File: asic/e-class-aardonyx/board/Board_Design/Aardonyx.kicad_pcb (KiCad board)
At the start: 4 copper layers, 157.5 x 117.3 mm, 325 parts, among them J1 USB_B_6PIN, J10 Conn_1x6_F, J11 Conn_1x6_F, J12 Conn_1x3_M, J13 Conn_1x8_F, J14 Conn_1x6_F, J15 Conn_1x10, J16 Conn_1x8_F, J17 USB_OTG, J18 Conn_1x3_M, J19 Conn_1x3_M, J2 Conn_1x8, J3 Conn_1x3_M, J4 Conn_1x4, J5 PJ-202H PWRJACK, J6 Conn_1x3_M, J7 Conn_1x4, J8 Conn_1x3_M, J9 Conn_1x8, Q1 FDN339AN, SW1 SW_SPST, SW2 FSM2JSMAATR, SW3 SW_DIP_x03, U1 FT2232H, U10 TPS7A7002DDAR, U11 ADM1186, U13 TPS7A7002DDAR, U14 74AUP1G09GW, U15 SKT32E, U16 93LC56BT-I_OT, U2 IS42S32160F-TSOP2, U3 CDCE913PW, U4 TPS54627DDAR, U5 CAT24M01WI-GT3, U6 IS25LP256x-xM, U7 ADC128S102CIMTX/NOPB, U8 LSF0108PWR, U9 LSF0108PWR, Y1 12MHz, Y2 27MHz

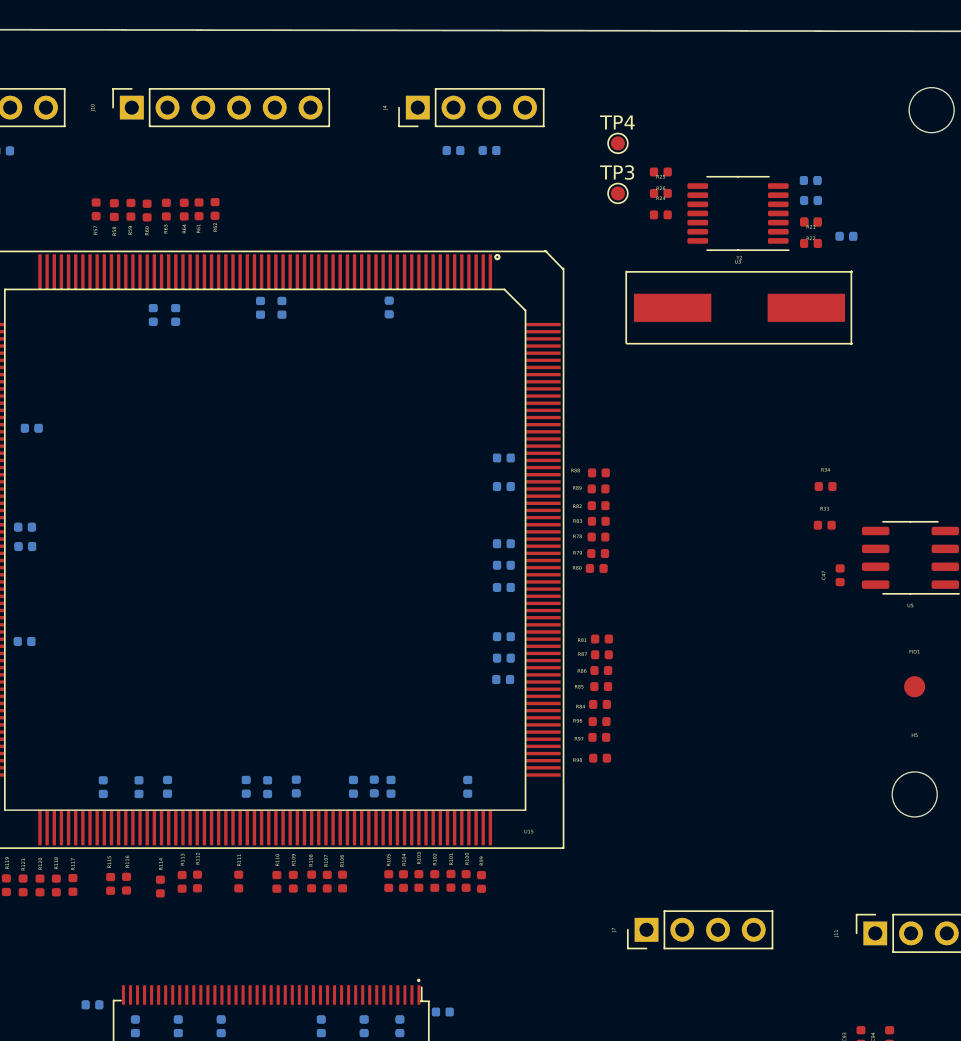
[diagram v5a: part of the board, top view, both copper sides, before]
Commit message: Updating 1x6 connector
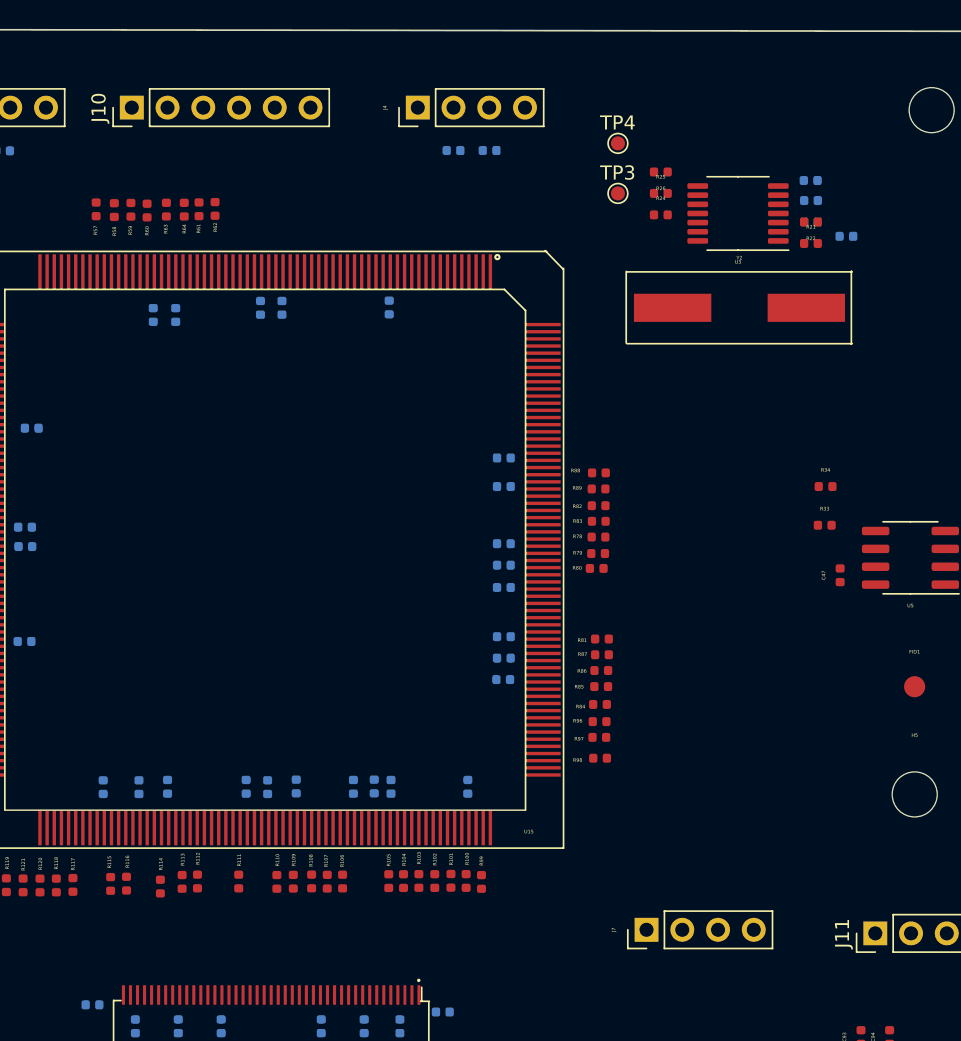
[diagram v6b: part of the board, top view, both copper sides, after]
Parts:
- J10, J11: value Conn_1x6_F -> Conn_1x6; footprint Connector_PinSocket_2.54mm:PinSocket_1x06_P2.54mm_Vertical -> Connector_PinHeader_2.54mm:PinHeader_1x06_P2.54mm_Vertical
- J15: value Conn_1x10 -> Conn_1x10_F
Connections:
- C30 pad 1: ~ -> V1P8
- C33 pad 1: ~ -> V12P0
- C34 pad 1: ~ -> V12P0
- C42 pad 1: ~ -> V12P0
- C44 pad 1: ~ -> V12P0
- C49 pad 1: ~ -> VAC
- C52 pad 1: ~ -> VREF_AH
- C54 pad 1: ~ -> VREF_AH
- J12 pad 2: ~ -> VREF_AH
- J13 pad 2: ~ -> Net-(J13-Pad2)
- J18 pad 2: ~ -> VBUS
- J19 pad 2: ~ -> VAC
- J6 pad 3: ~ -> VBUS
- L1 pad 4: ~ -> V12P0
- P_R25 pad 1: ~ -> V12P0
- R140 pad 1: V3P3 -> Net-(R140-Pad1)
- R22 pad 1: ~ -> V1P8
- R36 pad 1: ~ -> VREF_AH
- R37 pad 1: ~ -> VREF_AH
- R50 pad 1: ~ -> VBUS
- TP5 pad 1: ~ -> VCC5V
- U3 pad 3: ~ -> V1P8
- U4 pad 8: ~ -> V12P0
- U7 pad 2: ~ -> VAC
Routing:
- net ~: track 27.6 -> 0.00 mm
- net V12P0: track 0.00 -> 27.6 mm

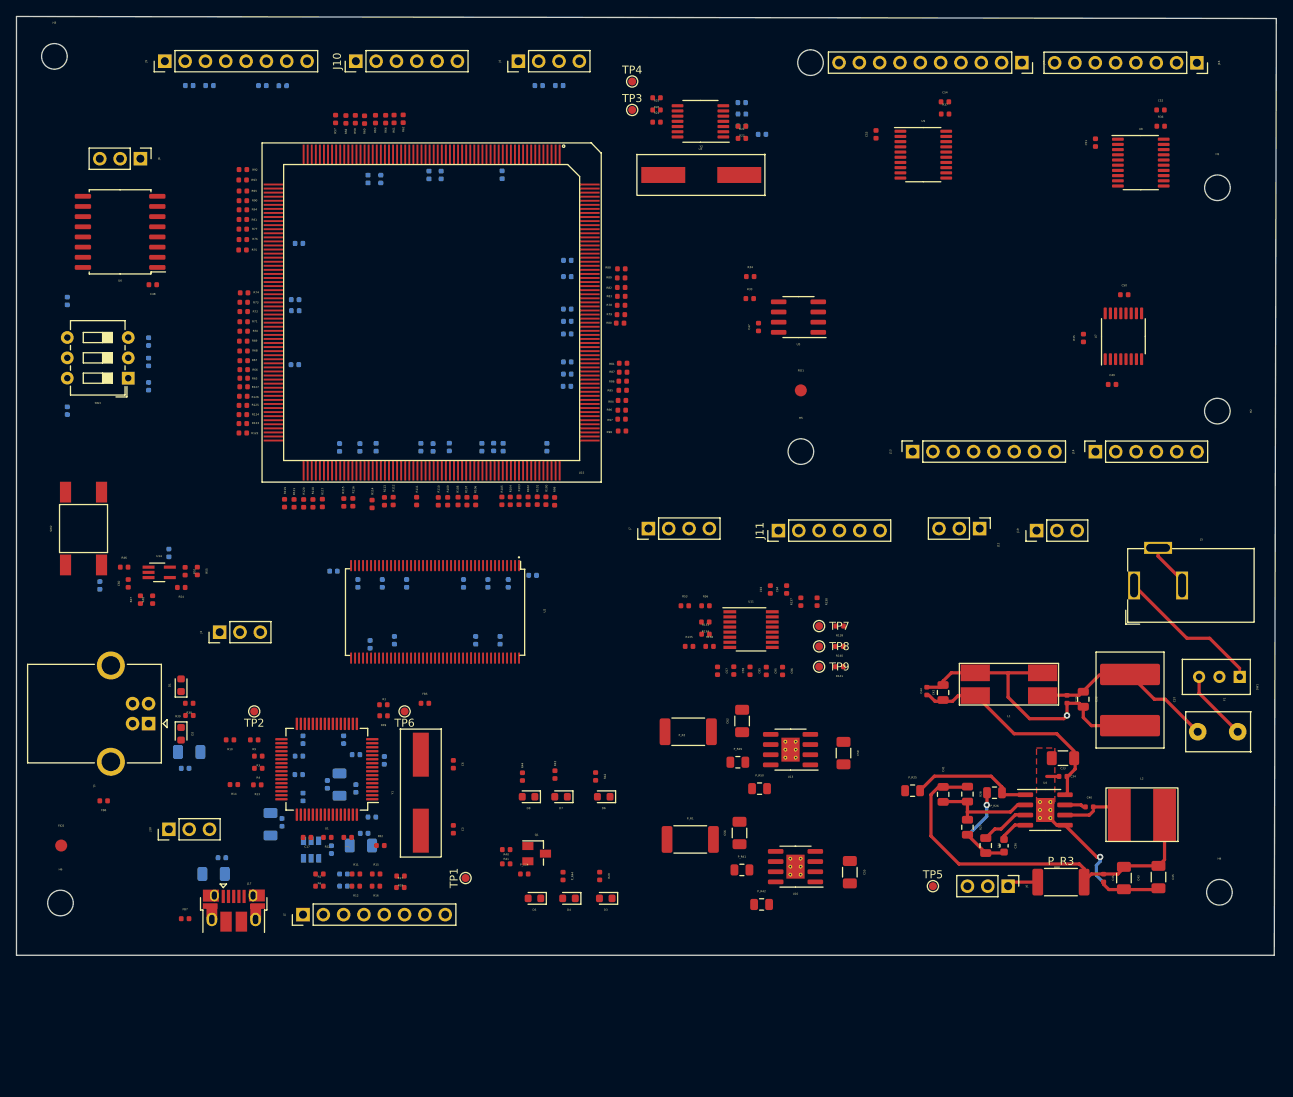
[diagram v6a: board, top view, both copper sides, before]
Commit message: updated track placement
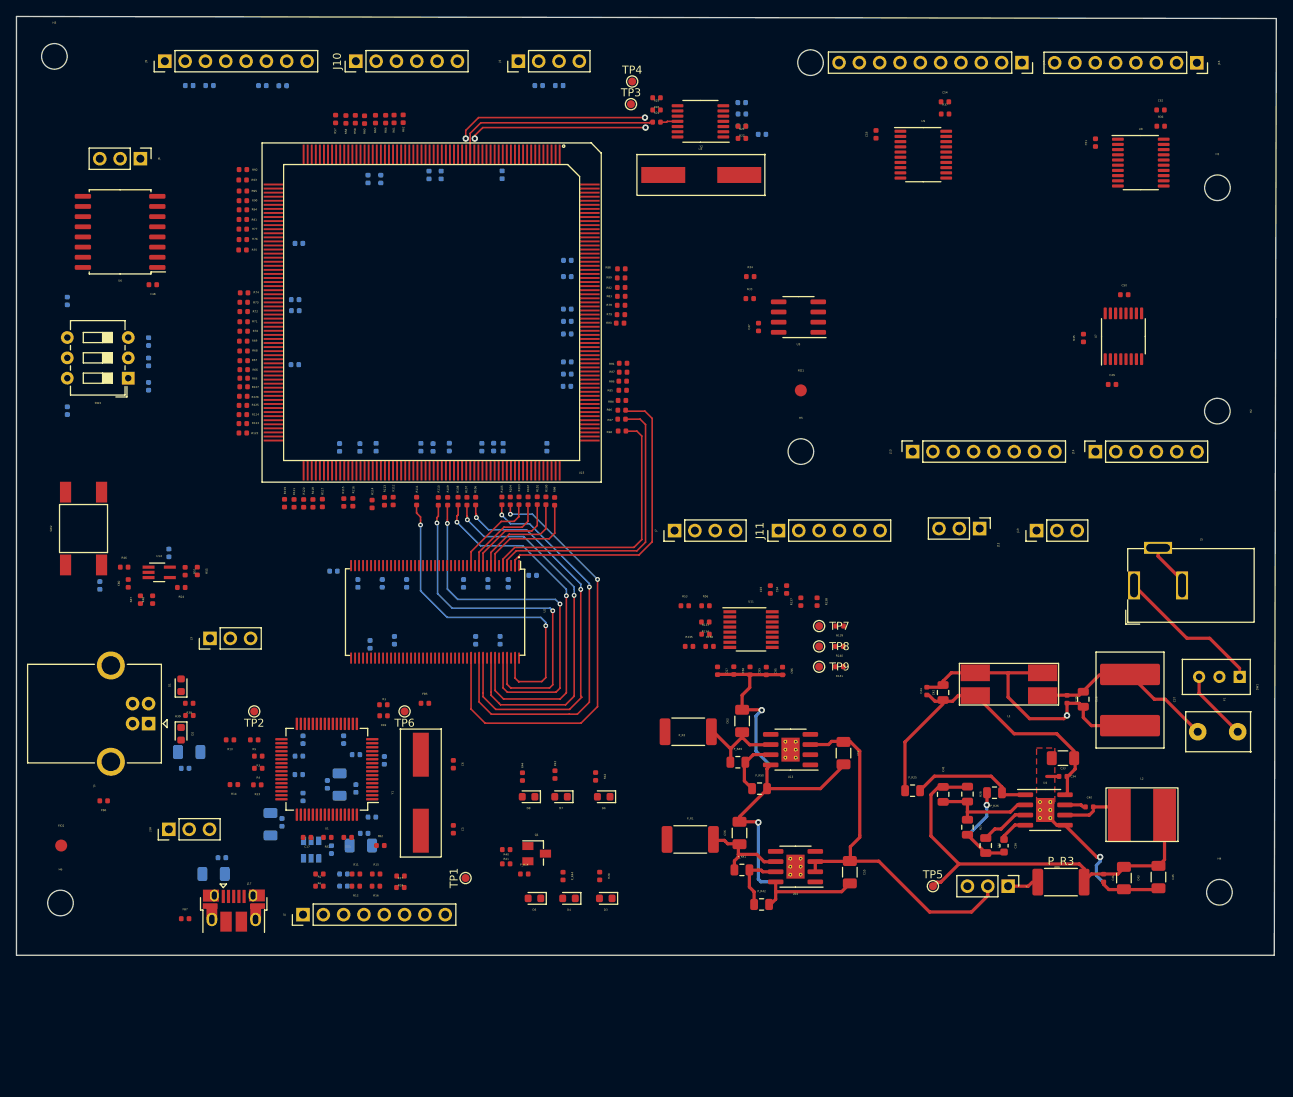
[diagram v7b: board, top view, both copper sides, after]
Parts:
- moved J7 3.28 mm to (205.4, 109.5)
- moved J3 1.44 mm to (147.4, 123.0)
- moved TP3 0.74 mm to (200.0, 56.2)
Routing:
- net GND: track 76.5 -> 190.6 mm, vias 3 -> 9
- net /sdram/SDRAM_D8: track 0.00 -> 56.0 mm, vias 0 -> 2
- net /sdram/SDRAM_D9: track 0.00 -> 51.8 mm, vias 0 -> 2
- net /sdram/SDRAM_D10: track 0.00 -> 51.4 mm, vias 0 -> 2
- net /sdram/SDRAM_D11: track 0.00 -> 49.0 mm, vias 0 -> 2
- net V5P0: track 0.00 -> 48.2 mm
- net /sdram/SDRAM_D13: track 0.00 -> 47.8 mm, vias 0 -> 2
- net /sdram/SDRAM_D12: track 0.00 -> 46.8 mm, vias 0 -> 2
- net /sdram/SDRAM_D14: track 0.00 -> 45.6 mm, vias 0 -> 2
- net /sdram/SDRAM_D15: track 0.00 -> 42.6 mm, vias 0 -> 2
- net /sdram/SDRAM_D0: track 0.00 -> 38.8 mm
- net /sdram/SDRAM_D1: track 0.00 -> 37.2 mm
- net /sdram/SDRAM_D2: track 0.00 -> 35.1 mm
- net /sdram/CLK: track 0.00 -> 27.2 mm
- net /sdram/SDRAM_D3: track 0.00 -> 14.2 mm
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
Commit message: udated track
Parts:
- moved C26 85.0 mm to (241.8, 82.8), turned to 180 degrees
- moved C27 83.2 mm to (241.3, 79.7), turned to 180 degrees
- moved C28 81.0 mm to (241.3, 69.6), turned to 180 degrees
- moved C29 80.9 mm to (241.3, 66.5), turned to 180 degrees
- moved U2 76.8 mm to (237.8, 74.6), turned to 0 degrees
- moved C24 75.4 mm to (234.2, 84.3), turned to 0 degrees
- moved C25 75.0 mm to (232.7, 87.3), turned to 270 degrees
- moved Y2 74.2 mm to (137.1, 84.0)
- moved C30 74.2 mm to (142.1, 77.9)
- moved C31 74.2 mm to (142.1, 76.4)
- moved C32 74.2 mm to (142.1, 75.0)
- moved R21 74.2 mm to (142.1, 79.5)
- moved R22 74.2 mm to (142.1, 77.9)
- moved R23 74.2 mm to (144.7, 79.0)
- moved R24 74.2 mm to (131.5, 77.4)
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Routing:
- net /sdram/SDRAM_D16: track 0.00 -> 84.9 mm, vias 0 -> 2
- net /sdram/SDRAM_D26: track 0.00 -> 84.1 mm, vias 0 -> 2
- net /sdram/SDRAM_D31: track 0.00 -> 84.1 mm, vias 0 -> 2
- net /sdram/SDRAM_D27: track 0.00 -> 84.0 mm, vias 0 -> 2
- net /sdram/SDRAM_D25: track 0.00 -> 83.9 mm
- net /sdram/SDRAM_D20: track 0.00 -> 83.9 mm, vias 0 -> 2
- net /sdram/SDRAM_D17: track 0.00 -> 83.9 mm, vias 0 -> 2
- net /sdram/SDRAM_D21: track 0.00 -> 83.9 mm, vias 0 -> 2
- net /sdram/SDRAM_D18: track 0.00 -> 83.9 mm, vias 0 -> 2
- net /sdram/SDRAM_D23: track 0.00 -> 83.9 mm, vias 0 -> 2
- net /sdram/SDRAM_D28: track 0.00 -> 83.9 mm, vias 0 -> 2
- net /sdram/SDRAM_D24: track 0.00 -> 83.9 mm
- net /sdram/SDRAM_D30: track 0.00 -> 83.9 mm, vias 0 -> 2
- net /sdram/SDRAM_D29: track 0.00 -> 83.9 mm, vias 0 -> 2
- net /sdram/SDRAM_D22: track 0.00 -> 83.8 mm, vias 0 -> 2
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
